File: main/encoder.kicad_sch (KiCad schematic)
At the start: 5 parts, among them J6 enc_host, J7 enc_slave, U6 AS5055A

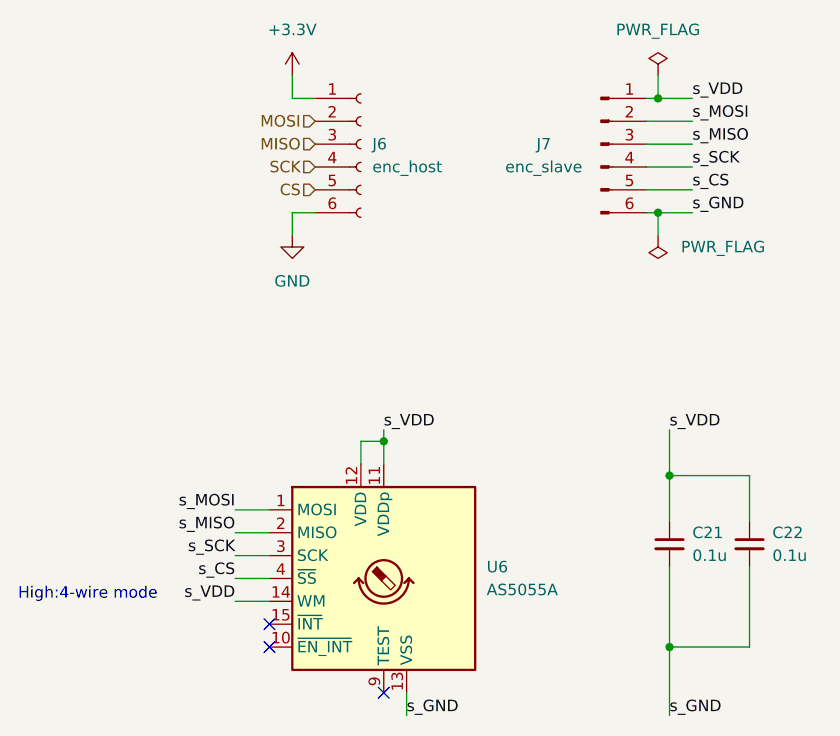
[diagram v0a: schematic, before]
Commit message: feat: update main board
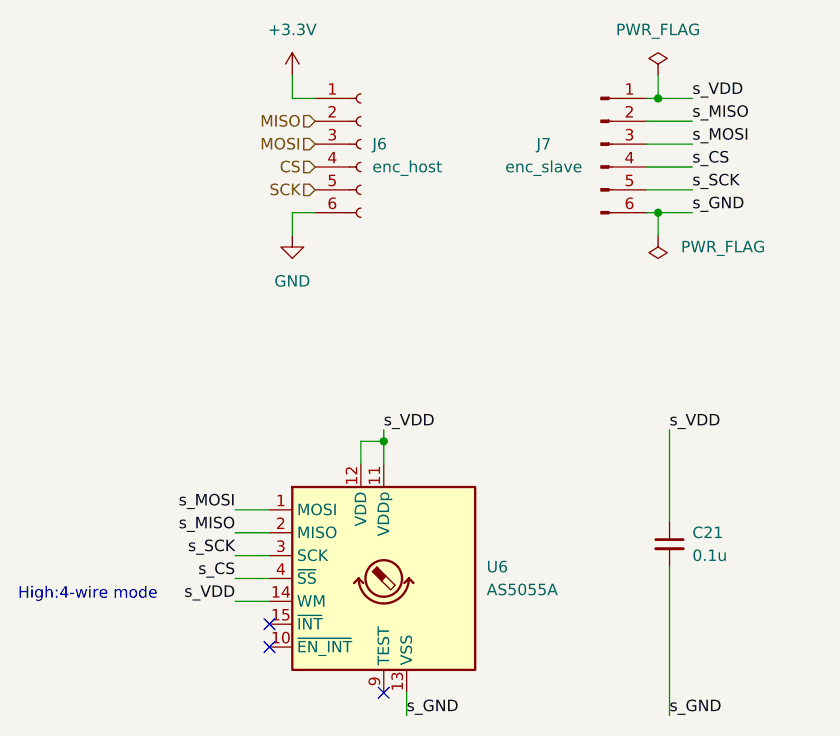
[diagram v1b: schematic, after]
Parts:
- removed C22: 0.1u, Capacitor_SMD:C_0201_0603Metric, symbol Device:C_Small
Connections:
- net CS: now also J6.4 (Pin_4); no longer J6.5 (Pin_5)
- net MISO: now also J6.2 (Pin_2); no longer J6.3 (Pin_3)
- net MOSI: now also J6.3 (Pin_3); no longer J6.2 (Pin_2)
- net SCK: now also J6.5 (Pin_5); no longer J6.4 (Pin_4)
- net s_CS: now also J7.4 (Pin_4); no longer J7.5 (Pin_5)
- net s_MISO: now also J7.2 (Pin_2); no longer J7.3 (Pin_3)
- net s_MOSI: now also J7.3 (Pin_3); no longer J7.2 (Pin_2)
- net s_SCK: now also J7.5 (Pin_5); no longer J7.4 (Pin_4)
